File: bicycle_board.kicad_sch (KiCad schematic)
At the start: 48 parts, among them J1 Micro_SD_Card, J10 USB_A, J11 Conn_01x04, J13 Conn_01x04, J2 USB_C_Receptacle_USB2.0_16P, J5 Conn_01x08, J6 Conn_01x04, J7 Conn_01x05, J8 Conn_01x02, J9 Conn_01x06, Q1 Q_NMOS_GSD, Q4 Q_NMOS_GSD, Q9 Q_PMOS_GSD, U13 NS4168, U14 ESP32-C3-WROOM-02U, U15 CH32V203C8T6, U7 74HC595, Y1 12MHz, Y2 32.768kHz

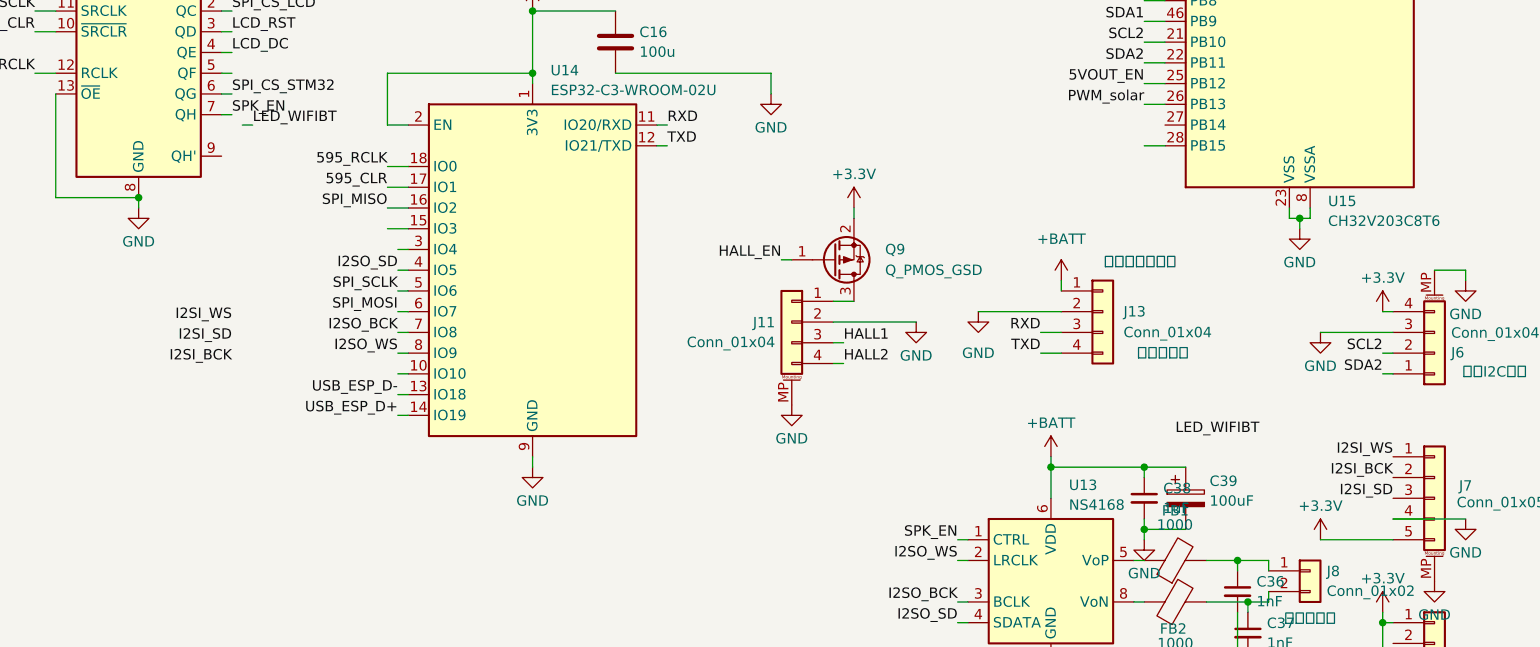
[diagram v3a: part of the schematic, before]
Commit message: 连接ESP32和I2S麦克风接口
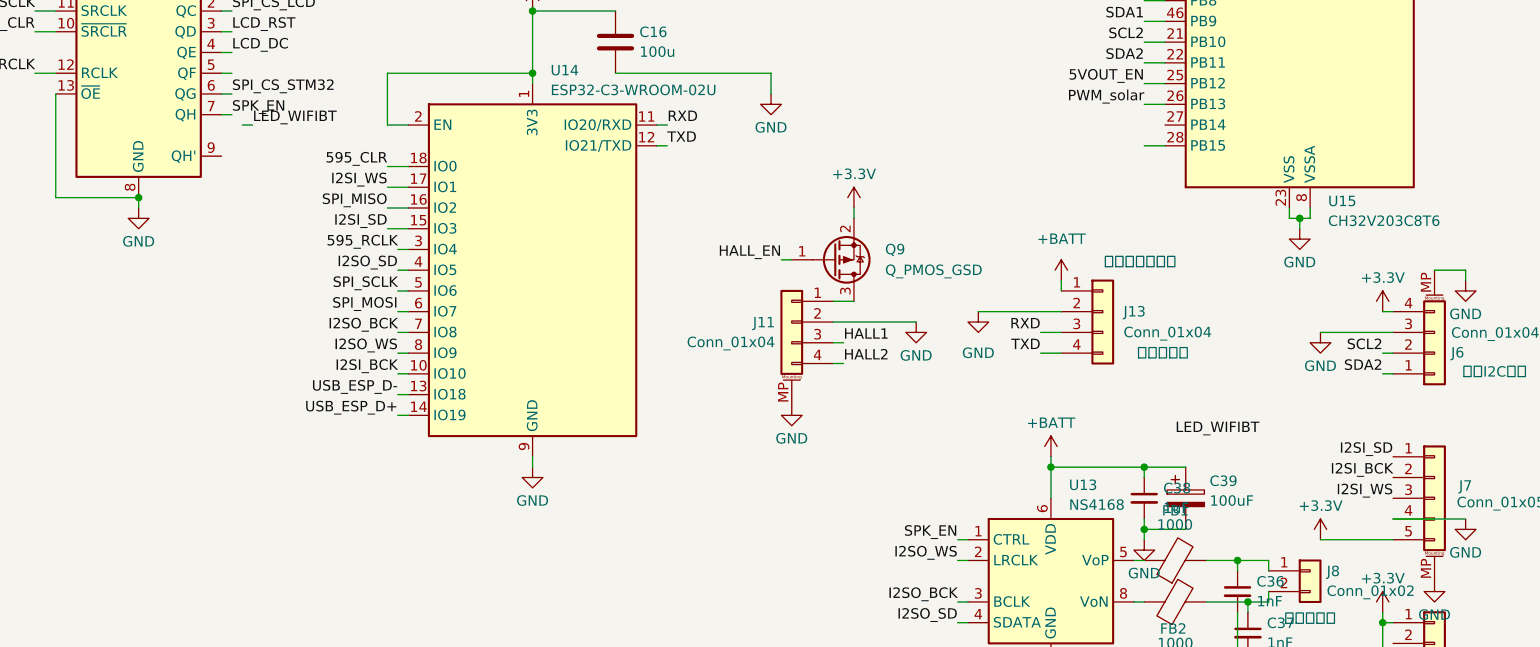
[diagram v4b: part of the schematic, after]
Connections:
- net 595_CLR: now also U14.18 (IO0); no longer U14.17 (IO1)
- net 595_RCLK: now also U14.3 (IO4); no longer U14.18 (IO0)
- net I2SI_BCK: now also U14.10 (IO10)
- net I2SI_SD: now also J7.1 (Pin_1), U14.15 (IO3); no longer J7.3 (Pin_3)
- net I2SI_WS: now also J7.3 (Pin_3), U14.17 (IO1); no longer J7.1 (Pin_1)
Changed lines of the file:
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@@
+		)
+	)
+	(label "595_CLR"
+		(at 146.05 97.79 180)
+		(fields_autoplaced yes)
+		(effects
+			(font
+				(size 1.27 1.27)
+			)
+			(justify right bottom)
 		)
 	)
@@
 		)
 	)
+	(label "I2SI_WS"
+		(at 146.05 100.33 180)
+		(fields_autoplaced yes)
+		(effects
+			(font
+				(size 1.27 1.27)
+			)
+			(justify right bottom)
+		)
+	)
 	(label "HALL_EN"
 		(at 276.86 46.99 0)
@@
 	)
 	(label "I2SI_WS"
-		(at 269.24 133.35 180)
+		(at 269.24 138.43 180)
 		(fields_autoplaced yes)
 		(effects
@@
 		)
 	)
+	(label "I2SI_BCK"
+		(at 147.32 123.19 180)
+		(fields_autoplaced yes)
+		(effects
+			(font
+				(size 1.27 1.27)
+			)
+			(justify right bottom)
+		)
+	)
 	(label "SCL1"
 		(at 238.76 77.47 180)
@@
 		)
 	)
+	(label "595_RCLK"
+		(at 147.32 107.95 180)
+		(fields_autoplaced yes)
+		(effects
+			(font
+				(size 1.27 1.27)
+			)
+			(justify right bottom)
+		)
+	)
 	(label "USB_ESP_D+"
 		(at 147.32 128.27 180)
@@
 		)
 	)
+	(label "I2SI_SD"
+		(at 146.05 105.41 180)
+		(fields_autoplaced yes)
+		(effects
+			(font
+				(size 1.27 1.27)
+			)
+			(justify right bottom)
+		)
+	)
 	(label "LCD_DC"
 		(at 127 83.82 0)
@@
 	)
 	(label "I2SI_SD"
-		(at 269.24 138.43 180)
+		(at 269.24 133.35 180)
 		(fields_autoplaced yes)
 		(effects
@@
 		)
 	)
-	(label "I2SI_WS"
-		(at 127 116.84 180)
-		(fields_autoplaced yes)
-		(effects
-			(font
-				(size 1.27 1.27)
-			)
-			(justify right bottom)
-		)
-	)
 	(label "HALL2"
 		(at 276.86 31.75 0)
@@
 		)
 	)
-	(label "595_RCLK"
-		(at 146.05 97.79 180)
-		(fields_autoplaced yes)
-		(effects
-			(font
-				(size 1.27 1.27)
-			)
-			(justify right bottom)
-		)
-	)
 	(label "SPISen_MOSI_3V3"
 		(at 172.72 57.15 180)
@@
 		)
 	)
-	(label "I2SI_BCK"
-		(at 127 121.92 180)
-		(fields_autoplaced yes)
-		(effects
-			(font
-				(size 1.27 1.27)
-			)
-			(justify right bottom)
-		)
-	)
 	(label "SPISen_SCLK_3V3"
 		(at 172.72 59.69 180)
@@
 		)
 	)
-	(label "I2SI_SD"
-		(at 127 119.38 180)
-		(fields_autoplaced yes)
-		(effects
-			(font
-				(size 1.27 1.27)
-			)
-			(justify right bottom)
-		)
-	)
 	(label "SPISen_MOSI_3V3"
 		(at 240.03 69.85 180)
@@
 		(fields_autoplaced yes)
 		(effects
-			(font
-				(size 1.27 1.27)
-			)
-			(justify right bottom)
-		)
-	)
-	(label "595_CLR"
-		(at 146.05 100.33 180)
-		(fields_autoplaced yes)
-		(effects

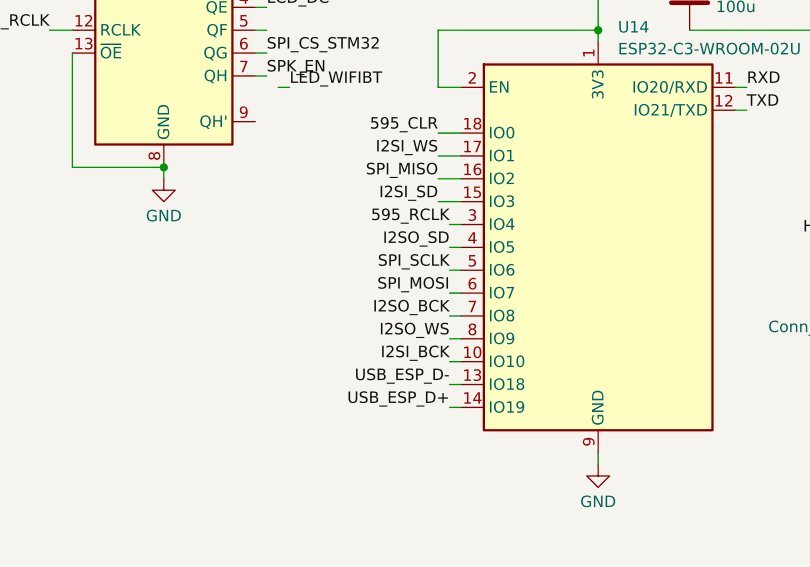
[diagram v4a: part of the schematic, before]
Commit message: 调整电源线宽度，一些走线布局
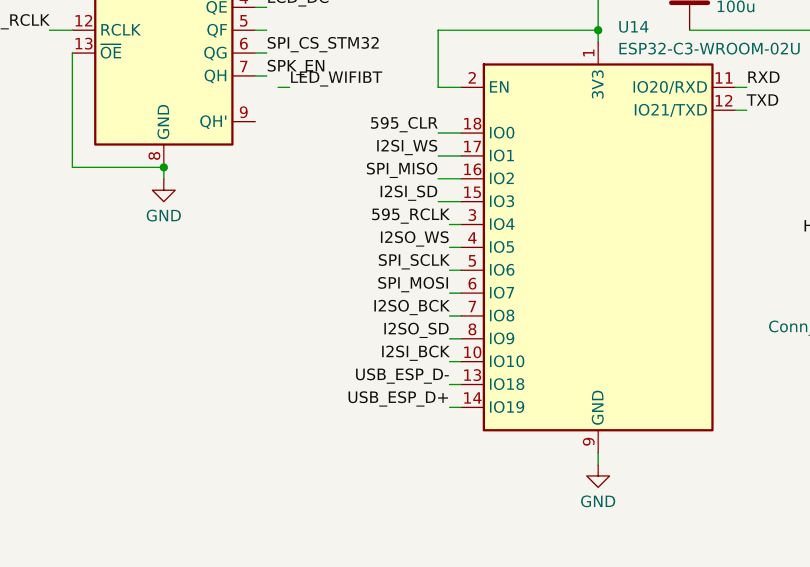
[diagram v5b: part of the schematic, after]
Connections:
- net I2SO_SD: now also U14.8 (IO9); no longer U14.4 (IO5)
- net I2SO_WS: now also U14.4 (IO5); no longer U14.8 (IO9)
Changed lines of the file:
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@@
 	)
 	(label "I2SO_SD"
-		(at 147.32 110.49 180)
+		(at 147.32 120.65 180)
 		(fields_autoplaced yes)
 		(effects
@@
 	)
 	(label "I2SO_WS"
-		(at 147.32 120.65 180)
+		(at 147.32 110.49 180)
 		(fields_autoplaced yes)
 		(effects

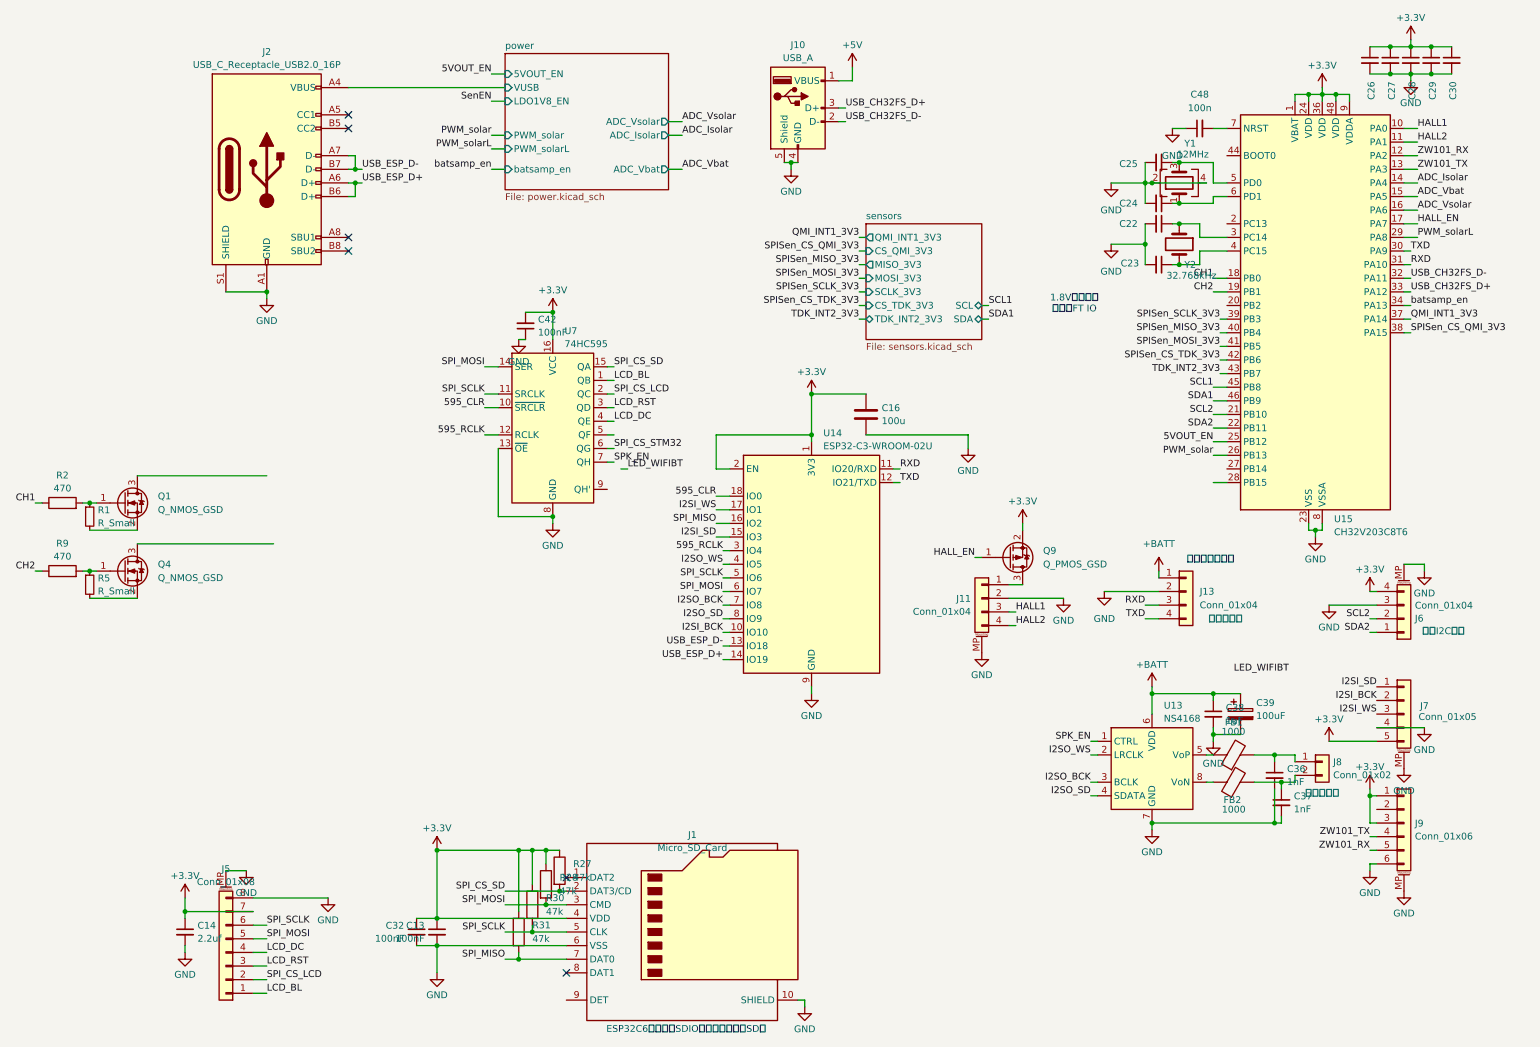
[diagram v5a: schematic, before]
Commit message: 接口添加TVS二极管和去耦电容，调整已有电容连接走线宽度
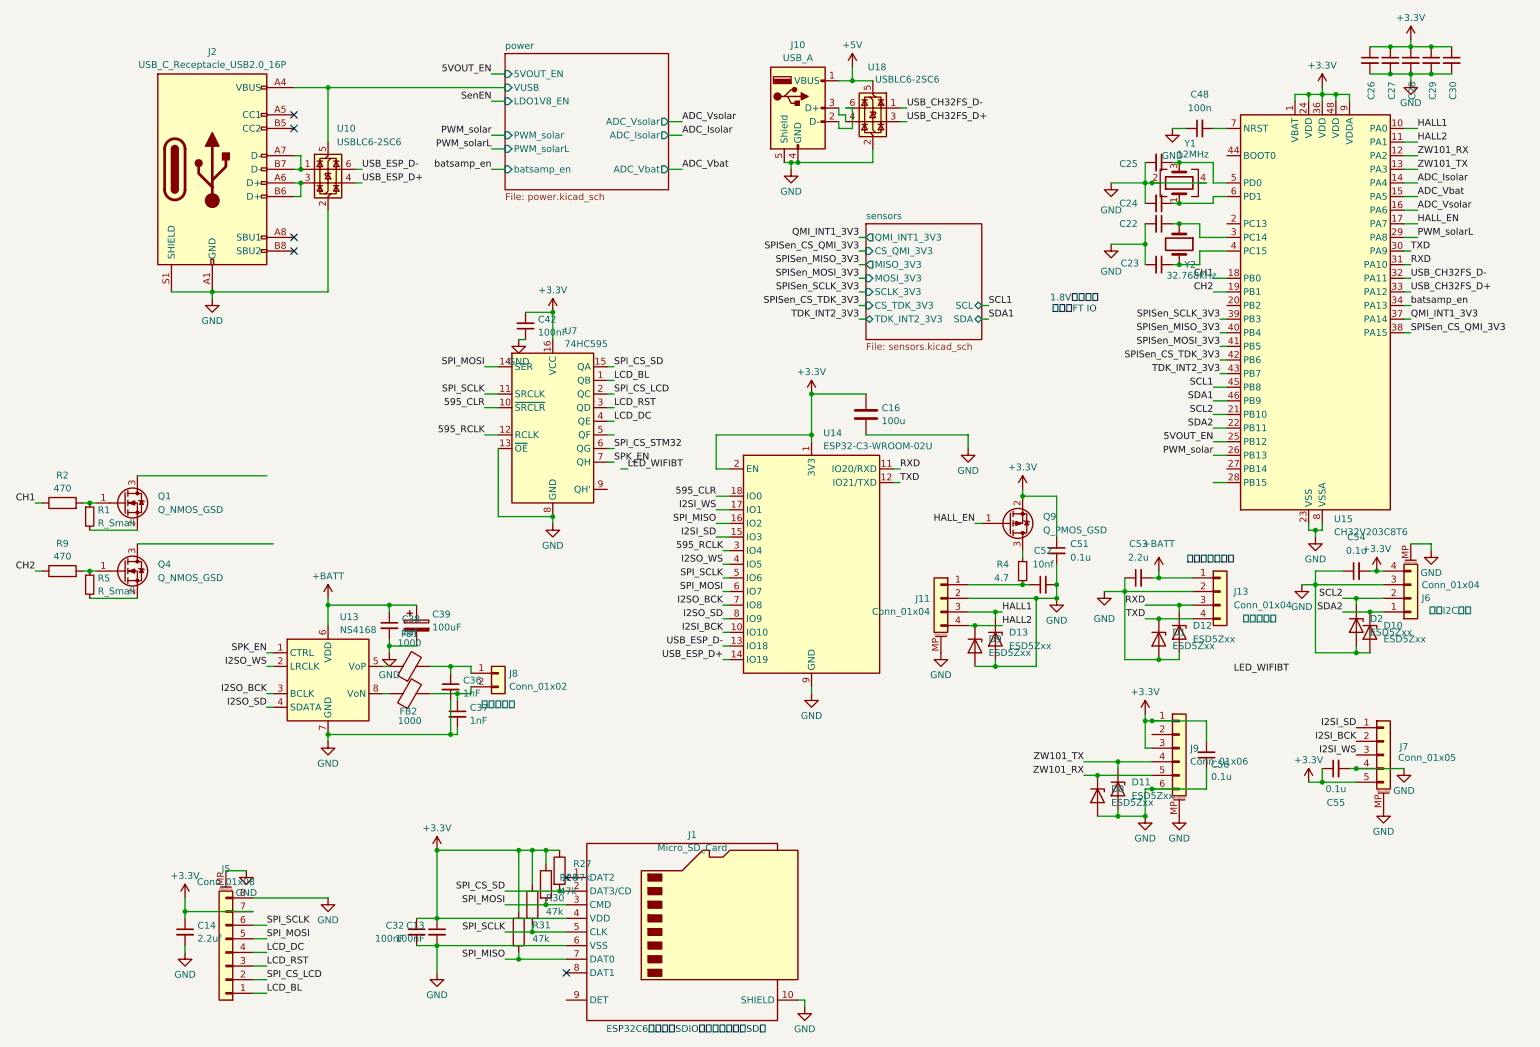
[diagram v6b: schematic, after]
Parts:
- added C51, C54, C55, C56: 0.1u, Capacitor_SMD:C_0402_1005Metric, symbol Device:C_Small
- added C52: 10nf, Capacitor_SMD:C_0402_1005Metric, symbol Device:C_Small
- added C53: 2.2u, Capacitor_SMD:C_0603_1608Metric, symbol Device:C_Small
- added D1, D10, D11, D12, D13, D2, D8, D9: ESD5Zxx, Diode_SMD:D_SOD-523, symbol Diode:ESD5Zxx
- added R4: 4.7, Resistor_SMD:R_0402_1005Metric, symbol Device:R_Small
- added U10, U18: USBLC6-2SC6, Package_TO_SOT_SMD:SOT-23-6, symbol Power_Protection:USBLC6-2SC6
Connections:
- net +3.3V: now also C51.1, C54.2, C55.1, C56.2
- net +5V: now also U18.5 (VBUS)
- net +BATT: now also C53.2
- net GND: now also C51.2, C52.2, C53.1, C54.1, C55.2, C56.1, D1.2 (A), D10.2 (A), D11.2 (A), D12.2 (A), D13.2 (A), D2.2 (A), D8.2 (A), D9.2 (A), U10.2 (GND), U18.2 (GND)
- net HALL1: now also D13.1 (K)
- net HALL2: now also D9.1 (K)
- net RXD: now also D12.1 (K)
- net SCL2: now also D2.1 (K)
- net SDA2: now also D10.1 (K)
- net TXD: now also D1.1 (K)
- net USB_CH32FS_D+: now also U18.3 (I/O2); no longer J10.3 (D+)
- net USB_CH32FS_D-: now also U18.1 (I/O1); no longer J10.2 (D-)
- net USB_ESP_D+: now also U10.4 (I/O2); no longer J2.A6 (D+), J2.B6 (D+)
- net USB_ESP_D-: now also U10.6 (I/O1); no longer J2.A7 (D-), J2.B7 (D-)
- net ZW101_RX: now also D8.1 (K)
- net ZW101_TX: now also D11.1 (K)
- net power/VUSB: now also U10.5 (VBUS)
- net at Q9.3 (D): now also R4.1; no longer J11.1 (Pin_1)
- new net: J2.A6 (D+), J2.B6 (D+), U10.3 (I/O2)
- new net: J2.A7 (D-), J2.B7 (D-), U10.1 (I/O1)
- new net: C52.1, J11.1 (Pin_1), R4.2
- new net: J10.2 (D-), U18.6 (I/O1)
- new net: J10.3 (D+), U18.4 (I/O2)
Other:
- moved on the sheet: C36, C37, C38, C39, FB1, FB2, J11, J13, J2, J6, J7, J8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

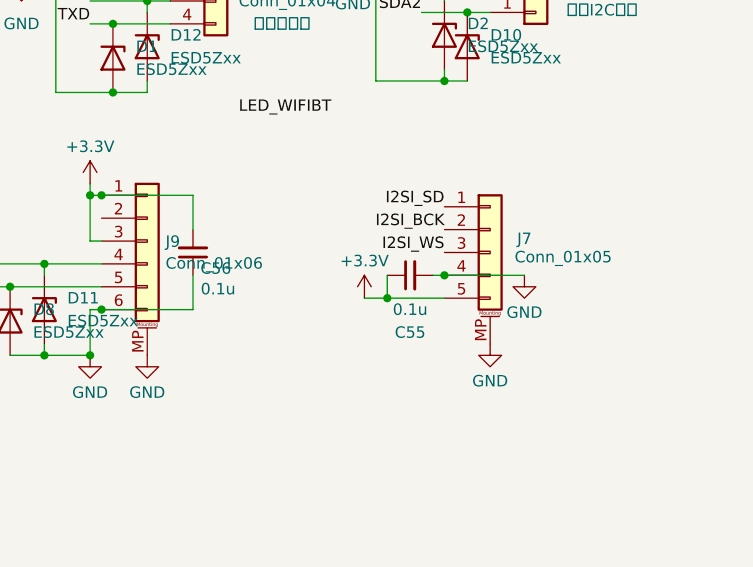
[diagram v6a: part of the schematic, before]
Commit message: I2S麦克风接口添加TVS管
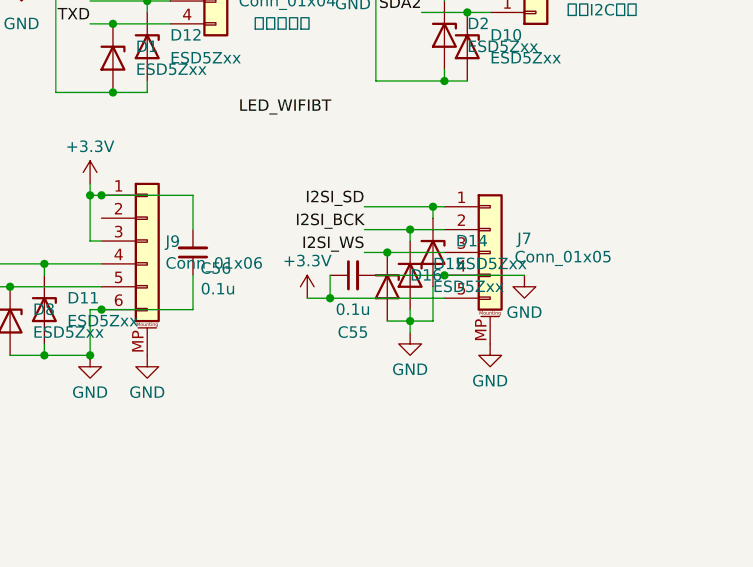
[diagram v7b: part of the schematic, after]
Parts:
- added D14, D15, D16: ESD5Zxx, Diode_SMD:D_SOD-523, symbol Diode:ESD5Zxx
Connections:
- net GND: now also D14.2 (A), D15.2 (A), D16.2 (A)
- net I2SI_BCK: now also D15.1 (K)
- net I2SI_SD: now also D14.1 (K)
- net I2SI_WS: now also D16.1 (K)
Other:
- moved on the sheet: C55

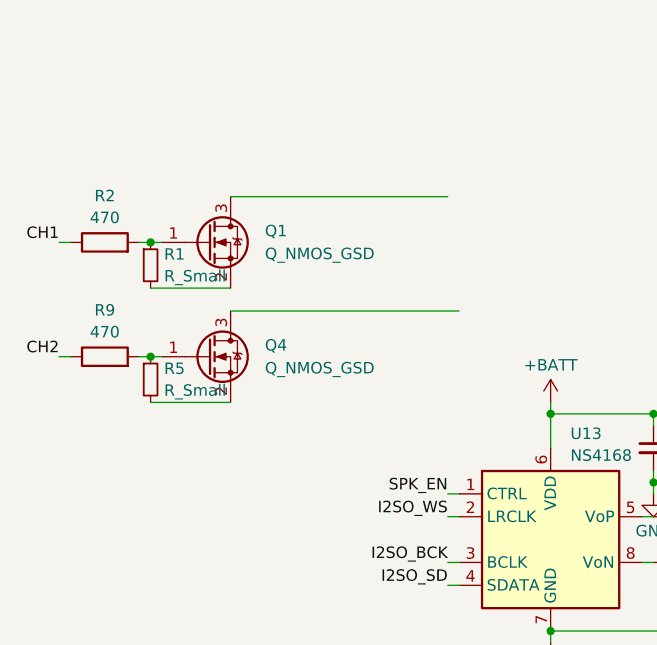
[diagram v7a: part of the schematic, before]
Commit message: 移动和微调MOS管通道电路并添加外接电路焊盘
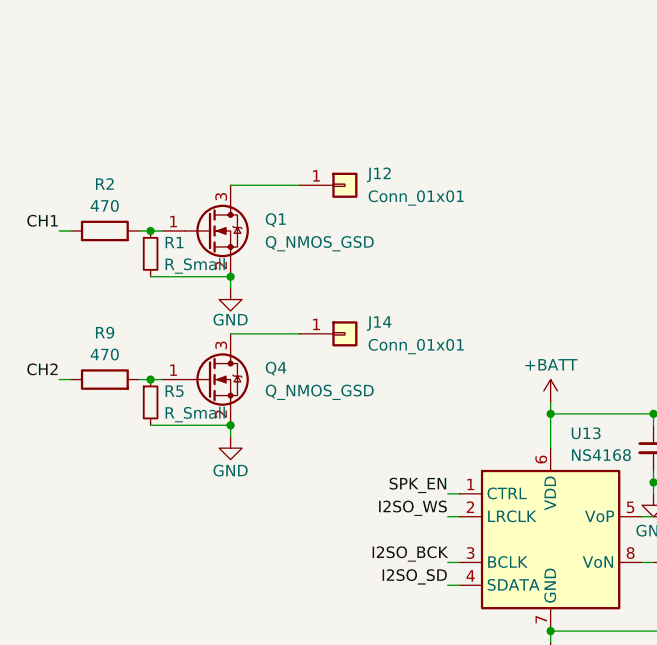
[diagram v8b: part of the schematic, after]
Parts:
- added J12, J14: Conn_01x01, TestPoint:TestPoint_Pad_D1.0mm, symbol Connector_Generic:Conn_01x01
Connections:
- net GND: now also Q1.2 (S), Q4.2 (S), R1.2, R5.2
- net at Q1.3 (D): now also J12.1 (Pin_1)
- net at Q4.3 (D): now also J14.1 (Pin_1)
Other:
- moved on the sheet: Q1, Q4, R1, R2, R5, R9
